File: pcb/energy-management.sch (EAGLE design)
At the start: 83 parts, among them IC2 74LS595D, IC3 74LS595D, J1 WIRE_HOLE-14AWG, J2 WIRE_HOLE-14AWG, J3 WIRE_HOLE-14AWG, J4 WIRE_HOLE-14AWG, U1 DS1307

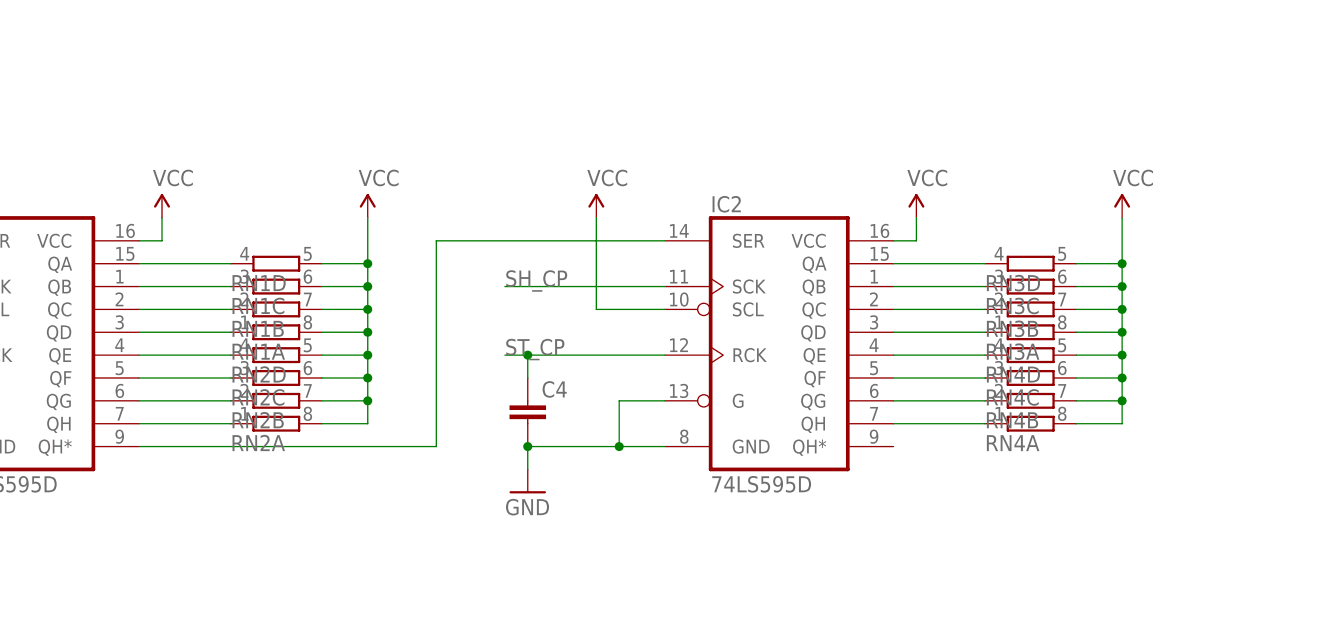
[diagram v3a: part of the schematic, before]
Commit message: remove resistor and cutout on analog line
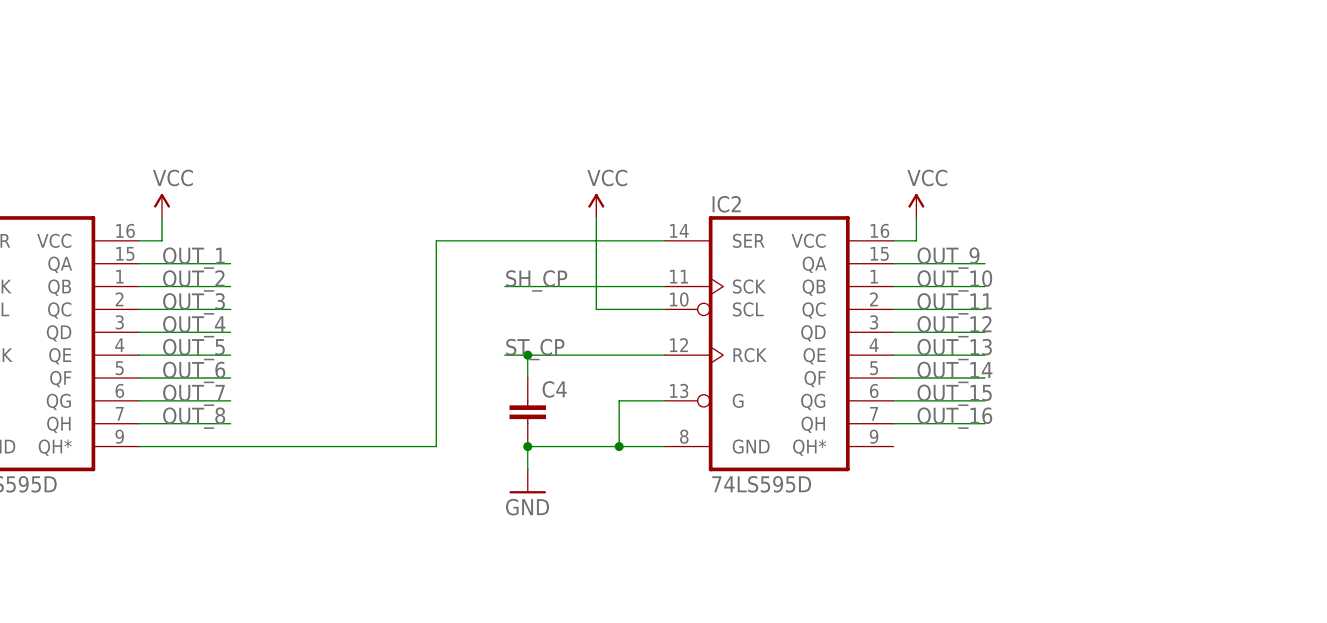
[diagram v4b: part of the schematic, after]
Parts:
- removed RN1, RN2, RN3, RN4: (no value), resistor-dil:4R-N0603-ARC
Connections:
- net OUT_1: no longer RN1D.1
- net OUT_10: no longer RN3C.1
- net OUT_11: no longer RN3B.1
- net OUT_12: no longer RN3A.1
- net OUT_13: no longer RN4D.1
- net OUT_14: no longer RN4C.1
- net OUT_15: no longer RN4B.1
- net OUT_16: no longer RN4A.1
- net OUT_2: no longer RN1C.1
- net OUT_3: no longer RN1B.1
- net OUT_4: no longer RN1A.1
- net OUT_5: no longer RN2D.1
- net OUT_6: no longer RN2C.1
- net OUT_7: no longer RN2B.1
- net OUT_8: no longer RN2A.1
- net OUT_9: no longer RN3D.1
- net VCC: no longer RN1A.2, RN1B.2, RN1C.2, RN1D.2, RN2A.2, RN2B.2, RN2C.2, RN2D.2, RN3A.2, RN3B.2, RN3C.2, RN3D.2, RN4A.2, RN4B.2, RN4C.2, RN4D.2

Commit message: remove unnecessary sensing 2 circuit
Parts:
- removed R20, R22: R470K, resistor:R-EU_R0805
- removed R26, R6: R1K, resistor:R-EU_R0805
- removed R7: R499K, resistor:R-EU_R0805
- removed TP_V_SENSING_1: PTR1PAD1-13, testpad:PTR1PAD1-13
- C3: value (none) -> C10uF; device resistor:CPOL-EU140CLH-0810 -> resistor:C-EUC0805
- R4-100K, R5-100K: value R470K -> (none)
- renumbered R4 to R4-100K, R5 to R5-100K, TP_V_SENSING_2 to TP_V_SENSING
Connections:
- removed net N$18: L1.2, R7.1
- removed net N$24: C3.+, R20.1, R22.2, R26.1
- removed net V_SENSING_1: R26.2, TP_V_SENSING_1.TP, U$1.A1
- removed net V_SENSING_2: R25.2, TP_V_SENSING.TP, U$1.A2
- new net V_SENSING: R25.2, TP_V_SENSING.TP, U$1.A1
- net 3V3: now also L1.1; no longer R20.2, R4-100K.2
- net GND: now also C3.2; no longer R22.1
- net N$1: now also C3.1, L1.2, R4-100K.2; no longer C3.-, R6.1, R7.2
- net WALL_NEUTRAL: no longer R6.2
- net WALL_PHASE: no longer L1.1
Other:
- moved on the sheet: L1

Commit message: connect vcc to out
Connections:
- removed net N$30: JP2.9
- net VCC: now also JP2.9
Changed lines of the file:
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@@
 <grid distance="0.1" unitdist="inch" unit="inch" style="lines" multiple="1" display="no" altdistance="0.01" altunitdist="inch" altunit="inch"/>
 <layers>
-<layer number="1" name="Top" color="4" fill="1" visible="yes" active="no"/>
-<layer number="2" name="Route2" color="1" fill="3" visible="yes" active="no"/>
-<layer number="3" name="Route3" color="4" fill="3" visible="yes" active="no"/>
-<layer number="4" name="Route4" color="1" fill="4" visible="yes" active="no"/>
-<layer number="5" name="Route5" color="4" fill="4" visible="yes" active="no"/>
-<layer number="6" name="Route6" color="1" fill="8" visible="yes" active="no"/>
-<layer number="7" name="Route7" color="4" fill="8" visible="yes" active="no"/>
-<layer number="8" name="Route8" color="1" fill="2" visible="yes" active="no"/>
-<layer number="9" name="Route9" color="4" fill="2" visible="yes" active="no"/>
-<layer number="10" name="Route10" color="1" fill="7" visible="yes" active="no"/>
-<layer number="11" name="Route11" color="4" fill="7" visible="yes" active="no"/>
-<layer number="12" name="Route12" color="1" fill="5" visible="yes" active="no"/>
-<layer number="13" name="Route13" color="4" fill="5" visible="yes" active="no"/>
-<layer number="14" name="Route14" color="1" fill="6" visible="yes" active="no"/>
-<layer number="15" name="Route15" color="4" fill="6" visible="yes" active="no"/>
-<layer number="16" name="Bottom" color="1" fill="1" visible="yes" active="no"/>
-<layer number="17" name="Pads" color="2" fill="1" visible="yes" active="no"/>
-<layer number="18" name="Vias" color="2" fill="1" visible="yes" active="no"/>
-<layer number="19" name="Unrouted" color="6" fill="1" visible="yes" active="no"/>
-<layer number="20" name="Dimension" color="15" fill="1" visible="yes" active="no"/>
-<layer number="21" name="tPlace" color="7" fill="1" visible="yes" active="no"/>
-<layer number="22" name="bPlace" color="7" fill="1" visible="yes" active="no"/>
-<layer number="23" name="tOrigins" color="15" fill="1" visible="yes" active="no"/>
-<layer number="24" name="bOrigins" color="15" fill="1" visible="yes" active="no"/>
-<layer number="25" name="tNames" color="7" fill="1" visible="yes" active="no"/>
-<layer number="26" name="bNames" color="7" fill="1" visible="yes" active="no"/>
-<layer number="27" name="tValues" color="7" fill="1" visible="yes" active="no"/>
-<layer number="28" name="bValues" color="7" fill="1" visible="yes" active="no"/>
+<layer number="1" name="Top" color="4" fill="1" visible="no" active="no"/>
+<layer number="2" name="Route2" color="1" fill="3" visible="no" active="no"/>
+<layer number="3" name="Route3" color="4" fill="3" visible="no" active="no"/>
+<layer number="4" name="Route4" color="1" fill="4" visible="no" active="no"/>
+<layer number="5" name="Route5" color="4" fill="4" visible="no" active="no"/>
+<layer number="6" name="Route6" color="1" fill="8" visible="no" active="no"/>
+<layer number="7" name="Route7" color="4" fill="8" visible="no" active="no"/>
+<layer number="8" name="Route8" color="1" fill="2" visible="no" active="no"/>
+<layer number="9" name="Route9" color="4" fill="2" visible="no" active="no"/>
+<layer number="10" name="Route10" color="1" fill="7" visible="no" active="no"/>
+<layer number="11" name="Route11" color="4" fill="7" visible="no" active="no"/>
+<layer number="12" name="Route12" color="1" fill="5" visible="no" active="no"/>
+<layer number="13" name="Route13" color="4" fill="5" visible="no" active="no"/>
+<layer number="14" name="Route14" color="1" fill="6" visible="no" active="no"/>
+<layer number="15" name="Route15" color="4" fill="6" visible="no" active="no"/>
+<layer number="16" name="Bottom" color="1" fill="1" visible="no" active="no"/>
+<layer number="17" name="Pads" color="2" fill="1" visible="no" active="no"/>
+<layer number="18" name="Vias" color="2" fill="1" visible="no" active="no"/>
+<layer number="19" name="Unrouted" color="6" fill="1" visible="no" active="no"/>
+<layer number="20" name="Dimension" color="15" fill="1" visible="no" active="no"/>
+<layer number="21" name="tPlace" color="7" fill="1" visible="no" active="no"/>
+<layer number="22" name="bPlace" color="7" fill="1" visible="no" active="no"/>
+<layer number="23" name="tOrigins" color="15" fill="1" visible="no" active="no"/>
+<layer number="24" name="bOrigins" color="15" fill="1" visible="no" active="no"/>
+<layer number="25" name="tNames" color="7" fill="1" visible="no" active="no"/>
+<layer number="26" name="bNames" color="7" fill="1" visible="no" active="no"/>
+<layer number="27" name="tValues" color="7" fill="1" visible="no" active="no"/>
+<layer number="28" name="bValues" color="7" fill="1" visible="no" active="no"/>
 <layer number="29" name="tStop" color="7" fill="3" visible="no" active="no"/>
 <layer number="30" name="bStop" color="7" fill="6" visible="no" active="no"/>
@@
 <layer number="35" name="tGlue" color="7" fill="4" visible="no" active="no"/>
 <layer number="36" name="bGlue" color="7" fill="5" visible="no" active="no"/>
-<layer number="37" name="tTest" color="7" fill="1" visible="yes" active="no"/>
-<layer number="38" name="bTest" color="7" fill="1" visible="yes" active="no"/>
+<layer number="37" name="tTest" color="7" fill="1" visible="no" active="no"/>
+<layer number="38" name="bTest" color="7" fill="1" visible="no" active="no"/>
 <layer number="39" name="tKeepout" color="4" fill="11" visible="no" active="no"/>
 <layer number="40" name="bKeepout" color="1" fill="11" visible="no" active="no"/>
@@
 <layer number="44" name="Drills" color="7" fill="1" visible="no" active="no"/>
 <layer number="45" name="Holes" color="7" fill="1" visible="no" active="no"/>
-<layer number="46" name="Milling" color="3" fill="1" visible="yes" active="no"/>
-<layer number="47" name="Measures" color="7" fill="1" visible="yes" active="no"/>
-<layer number="48" name="Document" color="7" fill="1" visible="yes" active="no"/>
-<layer number="49" name="Reference" color="7" fill="1" visible="yes" active="no"/>
-<layer number="50" name="dxf" color="7" fill="1" visible="yes" active="no"/>
-<layer number="51" name="tDocu" color="7" fill="1" visible="yes" active="no"/>
-<layer number="52" name="bDocu" color="7" fill="1" visible="yes" active="no"/>
-<layer number="53" name="tGND_GNDA" color="7" fill="9" visible="yes" active="no"/>
-<layer number="54" name="bGND_GNDA" color="1" fill="9" visible="yes" active="no"/>
-<layer number="56" name="wert" color="7" fill="1" visible="yes" active="no"/>
-<layer number="57" name="tCAD" color="7" fill="1" visible="yes" active="no"/>
+<layer number="46" name="Milling" color="3" fill="1" visible="no" active="no"/>
+<layer number="47" name="Measures" color="7" fill="1" visible="no" active="no"/>
+<layer number="48" name="Document" color="7" fill="1" visible="no" active="no"/>
+<layer number="49" name="Reference" color="7" fill="1" visible="no" active="no"/>
+<layer number="50" name="dxf" color="7" fill="1" visible="no" active="no"/>
+<layer number="51" name="tDocu" color="7" fill="1" visible="no" active="no"/>
+<layer number="52" name="bDocu" color="7" fill="1" visible="no" active="no"/>
+<layer number="53" name="tGND_GNDA" color="7" fill="9" visible="no" active="no"/>
+<layer number="54" name="bGND_GNDA" color="1" fill="9" visible="no" active="no"/>
+<layer number="56" name="wert" color="7" fill="1" visible="no" active="no"/>
+<layer number="57" name="tCAD" color="7" fill="1" visible="no" active="no"/>
 <layer number="91" name="Nets" color="2" fill="1" visible="yes" active="yes"/>
 <layer number="92" name="Busses" color="1" fill="1" visible="yes" active="yes"/>
@@
 <junction x="353.06" y="27.94"/>
 </segment>
+<segment>
+<pinref part="JP2" gate="A" pin="9"/>
+<wire x1="411.48" y1="261.62" x2="401.32" y2="261.62" width="0.1524" layer="91"/>
+<pinref part="P+6" gate="1" pin="VCC"/>
+</segment>
 </net>
 <net name="SCL" class="0">
@@
 </segment>
 </net>
-<net name="N$30" class="0">
-<segment>
-<pinref part="JP2" gate="A" pin="9"/>
-<wire x1="411.48" y1="261.62" x2="401.32" y2="261.62" width="0.1524" layer="91"/>
-</segment>
-</net>

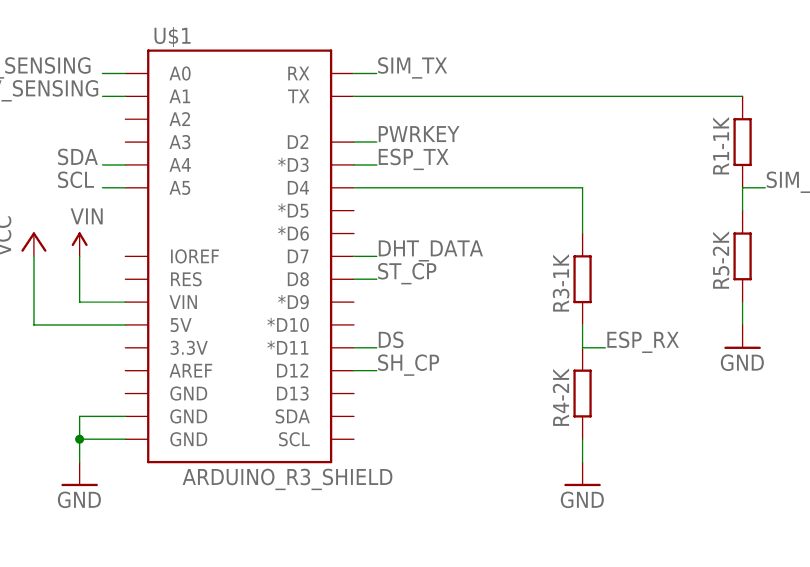
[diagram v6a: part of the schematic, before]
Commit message: update board
SH_CP and DS cannot be place on Eth pin
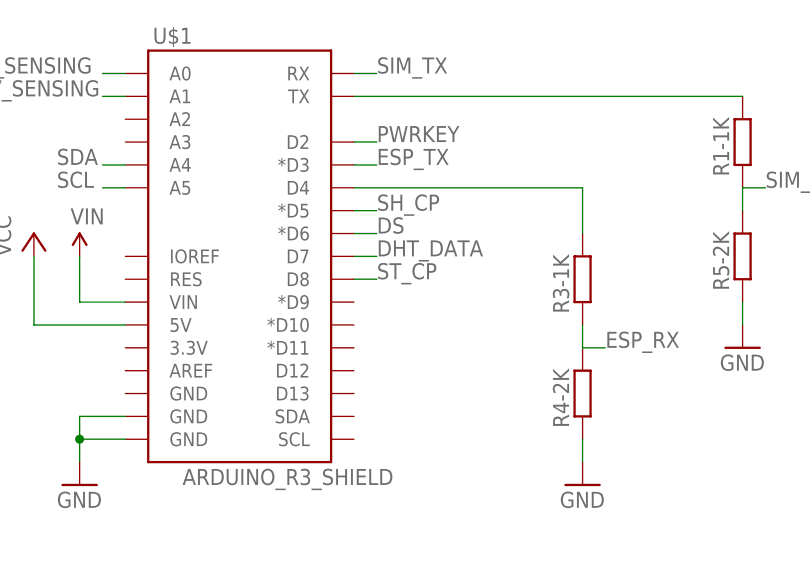
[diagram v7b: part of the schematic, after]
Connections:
- net DS: now also U$1.*D6; no longer U$1.*D11
- net SH_CP: now also U$1.*D5; no longer U$1.D12
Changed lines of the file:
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@@
 </segment>
 <segment>
-<pinref part="U$1" gate="G$1" pin="*D11"/>
-<wire x1="345.44" y1="66.04" x2="347.98" y2="66.04" width="0.1524" layer="91"/>
-<label x="347.98" y="66.04" size="1.778" layer="95"/>
+<pinref part="U$1" gate="G$1" pin="*D6"/>
+<wire x1="345.44" y1="78.74" x2="347.98" y2="78.74" width="0.1524" layer="91"/>
+<label x="347.98" y="78.74" size="1.778" layer="95"/>
 </segment>
 </net>
@@
 </segment>
 <segment>
-<pinref part="U$1" gate="G$1" pin="D12"/>
-<wire x1="345.44" y1="63.5" x2="347.98" y2="63.5" width="0.1524" layer="91"/>
-<label x="347.98" y="63.5" size="1.778" layer="95"/>
+<pinref part="U$1" gate="G$1" pin="*D5"/>
+<wire x1="345.44" y1="81.28" x2="347.98" y2="81.28" width="0.1524" layer="91"/>
+<label x="347.98" y="81.28" size="1.778" layer="95"/>
 </segment>
 </net>
